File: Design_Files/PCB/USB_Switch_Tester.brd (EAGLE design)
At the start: 32.4 x 16.5 mm, 7 parts, among them SW1 STX-3120

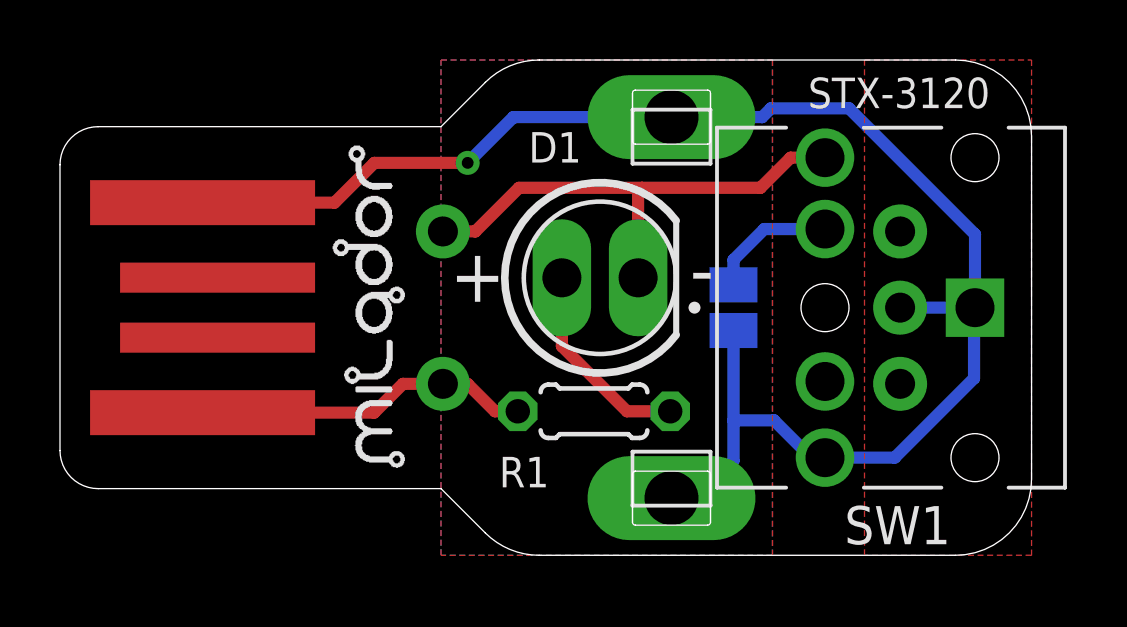
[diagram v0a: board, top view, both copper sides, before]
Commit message: Updated PCB: Added MMC Logo
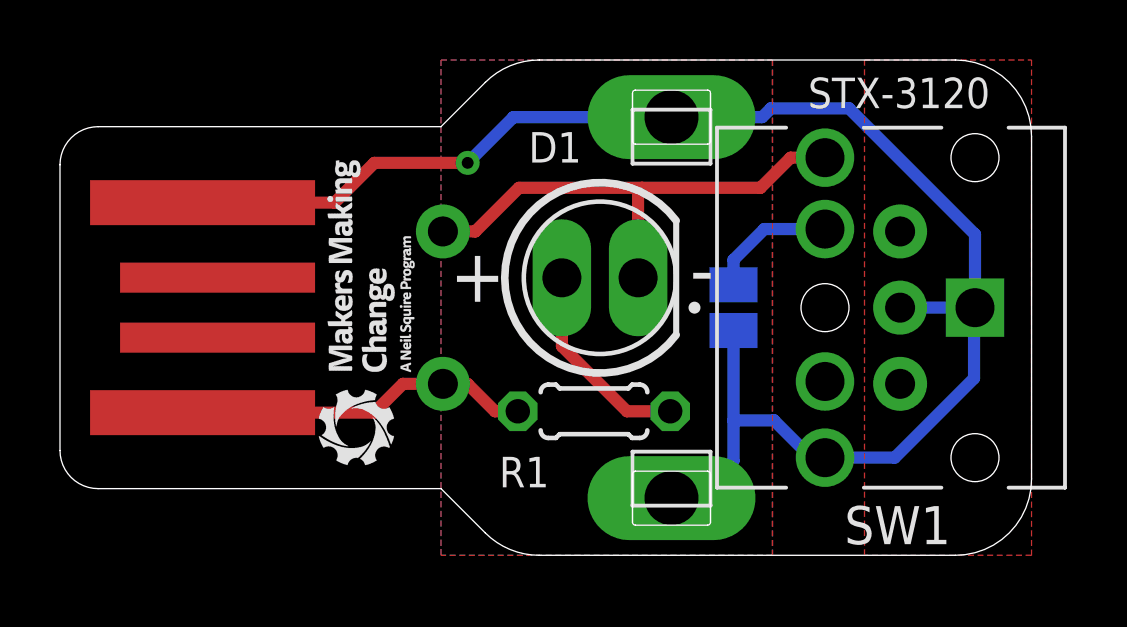
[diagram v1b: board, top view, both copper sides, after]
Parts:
- LABEL_LOGO: value MILADOR-LOGO-SM -> MMC_LOGO-XSM; device milador:MILADOR_LOGO2 -> MMC Eagle:MMC_X-SMALL_LOGO
- moved LABEL_LOGO 1.08 mm to (11.8, 8.00)
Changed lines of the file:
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@@
 <drawing>
 <settings>
-<setting alwaysvectorfont="no"/>
+<setting alwaysvectorfont="yes"/>
 <setting keepoldvectorfont="yes"/>
 <setting verticaltext="up"/>
@@
 </layers>
 <board>
-<fusionsync huburn="a.cGVyc29uYWw6dWUyYWQxOTI2" projecturn="a.cGVyc29uYWw6dWUyYWQxOTI2IzIwMjIwOTAyNTUxODYzODU2" f3durn="urn:adsk.wipprod:dm.lineage:fLiRhtAHSIeERth5YUiUTg" pcbguid="" lastpulledtime="" lastsyncedchangeguid="" latestrevisionid="f4c81e2b-8511-4f3d-8ff4-787618493aa6" lastsyncedrevisionid="f4c81e2b-8511-4f3d-8ff4-787618493aa6" lastboardhashguid="c153eb2f-9ae5-ac4f-7efe-45263b5d4bae" lastpushedtime="2022-09-02T04:23:09Z" linktopcb3d="false"/>
+<fusionsync huburn="a.cGVyc29uYWw6dWUyYWQxOTI2" projecturn="a.cGVyc29uYWw6dWUyYWQxOTI2IzIwMjIwOTAyNTUxODYzODU2" f3durn="urn:adsk.wipprod:dm.lineage:fLiRhtAHSIeERth5YUiUTg" pcbguid="" lastpulledtime="" lastsyncedchangeguid="" latestrevisionid="f4c81e2b-8511-4f3d-8ff4-787618493aa6" lastsyncedrevisionid="f4c81e2b-8511-4f3d-8ff4-787618493aa6" lastboardhashguid="c153eb2f-9ae5-ac4f-7efe-45263b5d4bae" lastpushedtime="2022-09-02T04:23:09Z" linktopcb3d="true"/>
 <plain>
 <wire x1="0" y1="13.0175" x2="1.27" y2="14.2875" width="0" layer="20" curve="-90"/>
@@
 <attribute name="VALUE" x="22.45" y="8.6551" size="0.02" layer="28" rot="MR90"/>
 </element>
-<element name="LABEL_LOGO" library="milador" library_urn="urn:adsk.eagle:library:12595918" package="MILADOR_LOGO2" package3d_urn="urn:adsk.eagle:package:36266468/1" value="MILADOR-LOGO-SM" x="10.8" y="7.6" smashed="yes" rot="R90"/>
+<element name="LABEL_LOGO" library="MMC Eagle" library_urn="urn:adsk.eagle:library:13126479" package="MMC_X-SMALL_LOGO" package3d_urn="urn:adsk.eagle:package:36433256/2" value="MMC_LOGO-XSM" x="11.8" y="8" smashed="yes" rot="R90"/>
 </elements>
 <signals>
